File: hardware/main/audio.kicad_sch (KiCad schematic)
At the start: 23 parts, among them J401 J_SPK_L, J402 J_SPK_R, J403 PJ-320D, U401 NS4150B, U402 NS4150B

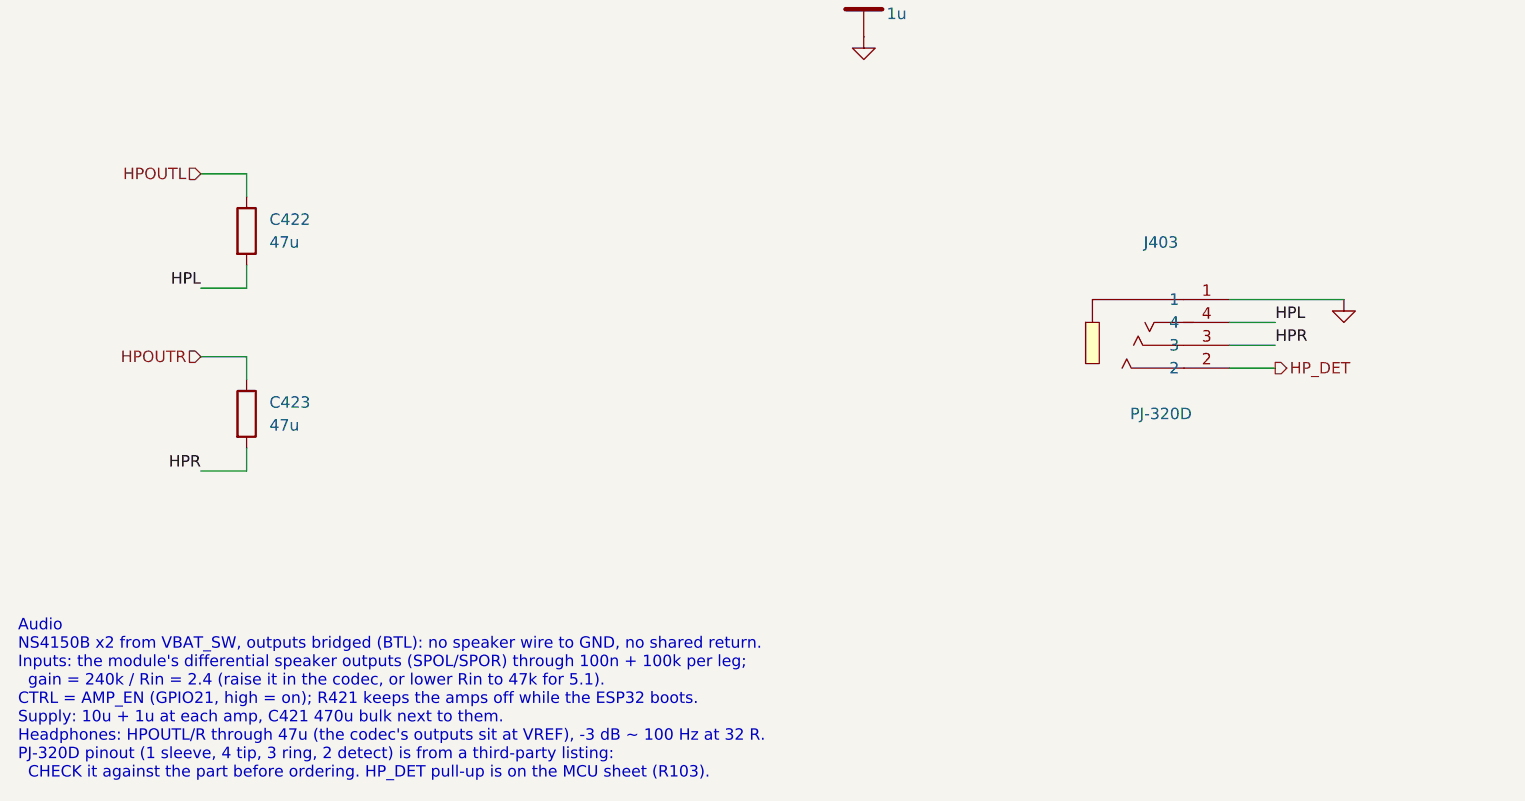
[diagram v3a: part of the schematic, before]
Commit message: hardware: headphone jack removed, main board 70 x 60 mm
- J403, C422, C423 out; HPOUTL/R open, GPIO39 spare with its pull-up.
- Main board re-placed on 70 x 60 mm (decoupling placed first), routed,
  labelled; route.py cleans dangling vias and sub-minimum tracks.
- LCSC fields rewritten after regenerating MCU and Audio sheets.

Co-Authored-By: Claude Opus 5.5 <noreply@anthropic.com>
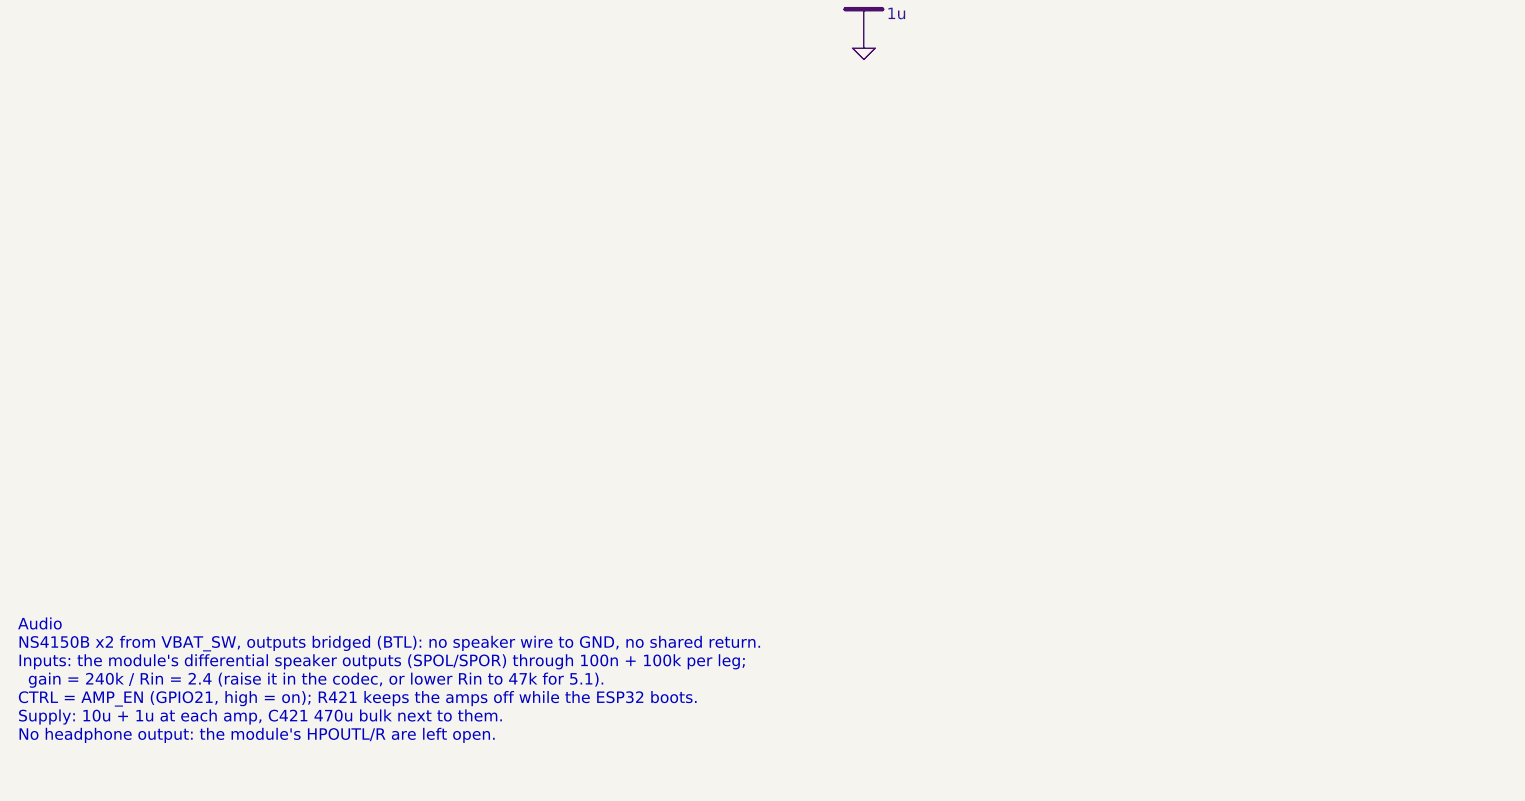
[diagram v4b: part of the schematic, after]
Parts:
- removed C422, C423: 47u, Capacitor_SMD:C_0805_2012Metric, symbol Device:R
- removed J403: PJ-320D, lcsc:AUDIO-SMD_PJ-320D-1, symbol lcsc:PJ-320D
